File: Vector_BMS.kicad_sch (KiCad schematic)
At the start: 217 parts, among them J1 CT3151V1-0, J10 CT3151V1-2, J11 CT3151V1-2, J13 CT3151V1-2, J15 CT3151V1-2, J16 Temp, J17 - Power +, J18 Conn_01x02_Pin, J2 Charger +, J20 Conn_01x02_Pin, J21 Conn_01x02_Pin, J23 Power Button, J27 CT3151V1-2, J28 CT3151V1-2, J29 CT3151V1-2, J30 CT3151V1-2, J31 CT3151V1-2, J32 CT3151V1-2, J33 CT3151V1-2, J34 CT3151V1-2, J35 CT3151V1-2, J36 CT3151V1-2, J37 CT3151V1-2, J38 CT3151V1-2, J39 CT3151V1-2, J4 Temp, J40 CT3151V1-2, J41 CT3151V1-2, J42 CT3151V1-2, J5 CT3151V1-2, J6 CT3151V1-2, J7 CT3151V1-2, J8 CT3151V1-2, J9 Conn_01x02_Pin, K1 HE3621A1200, Q1 NSV1C201MZ4, Q16 BSS138, Q18 BUK98150-55A, Q19 BUK98150-55A, Q2 NSV1C201MZ4, Q20 BUK98150-55A, Q22 BSS138, Q23 BSS138, Q24 BSS138, Q25 BSS138, U1 LTC6811-1, U2 LTC6811-1, U5 LM5165YDRC, U7 ISL28022, U8 SFH617A-2X009T, U9 CPC1019N

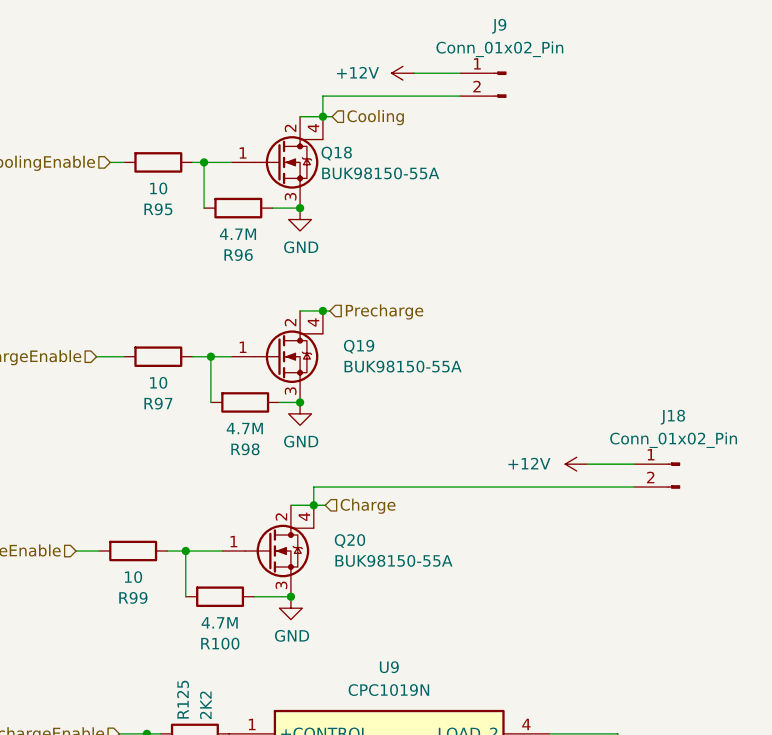
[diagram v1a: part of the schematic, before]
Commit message: Replace BUK98150-55A with IRFL4105PBF (Q18, Q19, Q20)
BUK98150-55A has limited availability. IRFL4105PBF is a drop-in replacement:
- Same package (SOT-223)
- Same voltage (55V)
- Lower Rds(on) (45mΩ vs 137mΩ)
- 3.7A vs 5.5A current rating
- In stock at DigiKey/Mouser
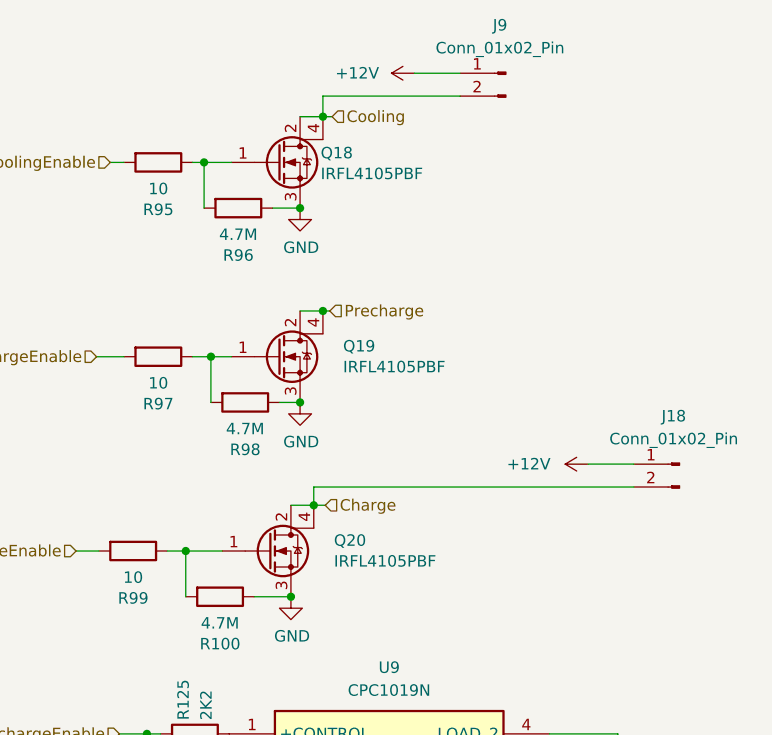
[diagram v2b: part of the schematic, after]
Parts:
- Q18, Q19, Q20: value BUK98150-55A -> IRFL4105PBF; MPN BUK98150-55A/CUF -> IRFL4105PBF

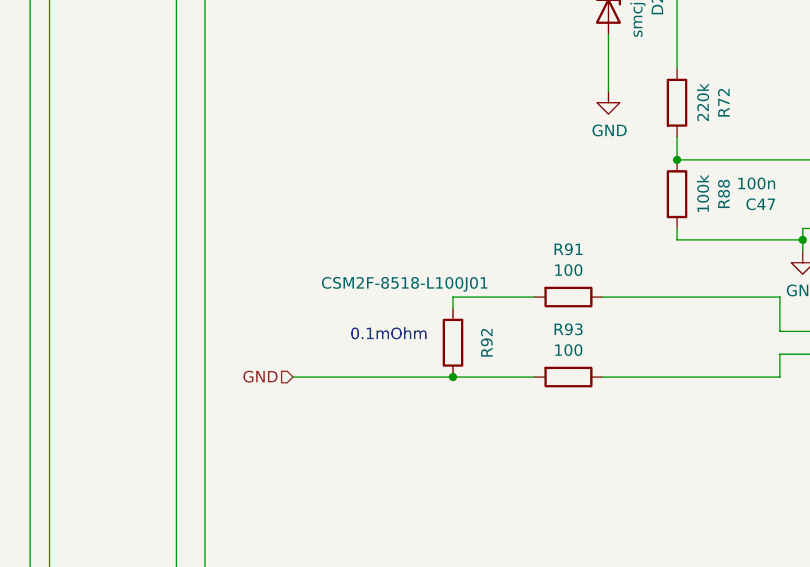
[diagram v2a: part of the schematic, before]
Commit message: Replace R92 shunt resistor with smaller WSLP5931L1000FEA
CSM2F-8518-L100J01 (85×18mm) → WSLP5931L1000FEA (15×7.6mm)
- Same resistance: 0.1mΩ
- 15W rating (plenty for 120A @ 1.44W)
- 5.6× smaller footprint
- Better tolerance: ±1% vs ±5%
- LCSC: $0.93
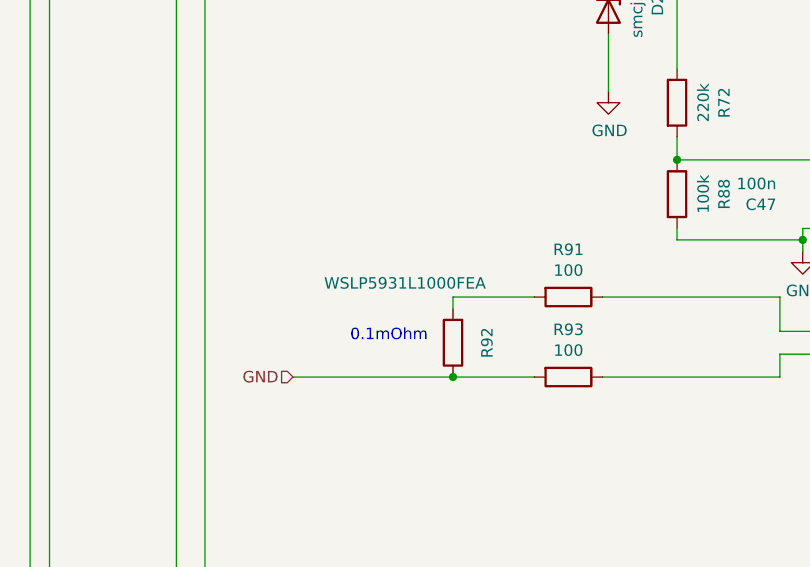
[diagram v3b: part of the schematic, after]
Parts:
- R92: value CSM2F-8518-L100J01 -> WSLP5931L1000FEA; footprint (none) -> Resistor_SMD:R_5931_15076Metric

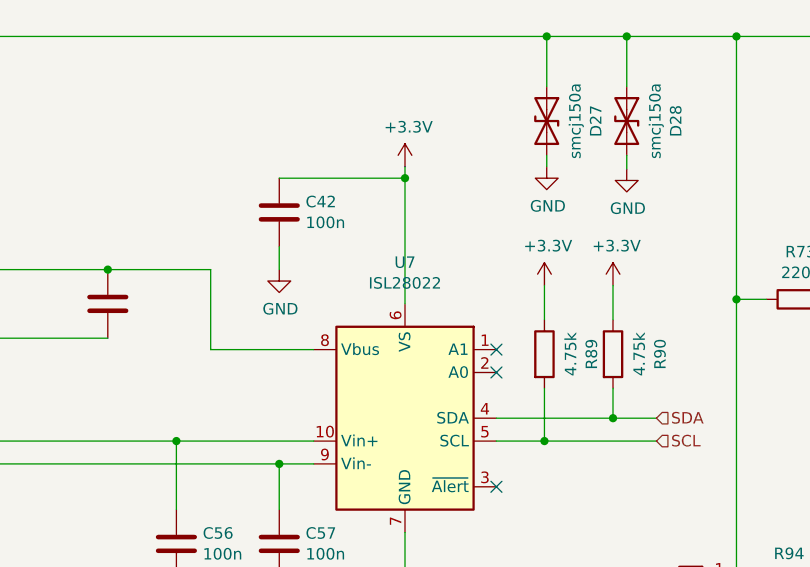
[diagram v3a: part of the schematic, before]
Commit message: Replace U7 ISL28022 (EOL) with INA226
ISL28022FUZ-T7A → INA226AIDGSR
- Pin-compatible drop-in replacement
- Same VSSOP-10 footprint
- Same I2C interface
- ISL28022 was EOL'd Dec 2019
- INA226 actively produced by TI
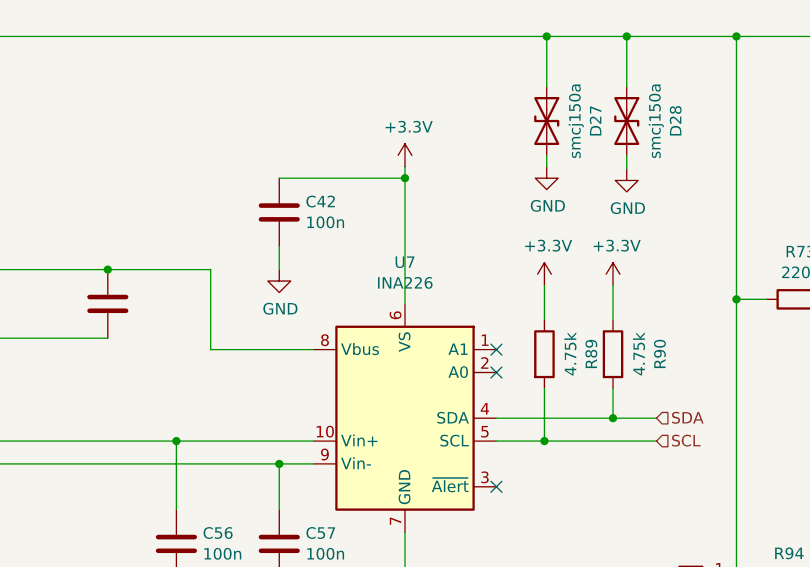
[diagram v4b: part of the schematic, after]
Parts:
- U7: value ISL28022 -> INA226; MPN ISL28022FUZ-T7A -> INA226AIDGSR
